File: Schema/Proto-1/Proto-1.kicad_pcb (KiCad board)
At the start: 2 copper layers, 71.5 x 29 mm, 5 parts, among them J1 Conn_02x03_Top_Bottom, U1 ATtiny85V-10P

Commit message: Benenne Files um
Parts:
- J1: value Conn_02x03_Top_Bottom -> Conn_02x03
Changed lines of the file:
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@@
 		)
 	)
-	(property "Version" "P1-0.3")
+	(property "Version" "P1-0.4a")
 	(net 0 "")
 	(net 1 "Net-(D1-DIN)")
@@
 		(property ki_fp_filters "DIP*W7.62mm*")
 		(sheetname "/")
-		(sheetfile "Spice.kicad_sch")
+		(sheetfile "Proto-1.kicad_sch")
 		(attr smd)
 		(fp_line
@@
 			)
 		)
-		(property "Value" "Conn_02x03_Top_Bottom"
+		(property "Value" "Conn_02x03"
 			(at 6.215 11.18 0)
 			(layer "F.Fab")
@@
 		(property ki_fp_filters "Connector*:*_2x??_*")
 		(sheetname "/")
-		(sheetfile "Spice.kicad_sch")
+		(sheetfile "Proto-1.kicad_sch")
 		(attr through_hole)
 		(fp_line
@@
 		(property ki_fp_filters "LED*WS2812*PLCC*5.0x5.0mm*P3.2mm*")
 		(sheetname "/")
-		(sheetfile "Spice.kicad_sch")
+		(sheetfile "Proto-1.kicad_sch")
 		(attr smd)
 		(fp_line
@@
 		(property ki_fp_filters "LED*WS2812*PLCC*5.0x5.0mm*P3.2mm*")
 		(sheetname "/")
-		(sheetfile "Spice.kicad_sch")
+		(sheetfile "Proto-1.kicad_sch")
 		(attr smd)
 		(fp_line
@@
 		(property ki_fp_filters "LED*WS2812*PLCC*5.0x5.0mm*P3.2mm*")
 		(sheetname "/")
-		(sheetfile "Spice.kicad_sch")
+		(sheetfile "Proto-1.kicad_sch")
 		(attr smd)
 		(fp_line

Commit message: Erstelle Schema für B
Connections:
- J1 pad 4: unconnected-(J1-Pin_4-Pad4) -> Reset
- U1 pad 1: unconnected-(U1-~{RESET}/PB5-Pad1) -> Reset
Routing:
- net Reset: track 0.00 -> 32.0 mm
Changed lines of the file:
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@@
 	(net 8 "SDA{slash}MOSI")
 	(net 9 "SCL{slash}MISO")
-	(net 10 "unconnected-(J1-Pin_4-Pad4)")
-	(net 11 "unconnected-(U1-~{RESET}{slash}PB5-Pad1)")
-	(net 12 "unconnected-(U1-XTAL2{slash}PB4-Pad3)")
+	(net 10 "Reset")
+	(net 11 "unconnected-(U1-XTAL2{slash}PB4-Pad3)")
 	(footprint "Package_SO:SO-8_3.9x4.9mm_P1.27mm"
 		(layer "F.Cu")
@@
 			(layers "F.Cu" "F.Mask" "F.Paste")
 			(roundrect_rratio 0.25)
-			(net 11 "unconnected-(U1-~{RESET}{slash}PB5-Pad1)")
+			(net 10 "Reset")
 			(pinfunction "~{RESET}/PB5")
-			(pintype "bidirectional+no_connect")
+			(pintype "bidirectional")
 		)
 		(pad "2" smd roundrect
@@
 			(layers "F.Cu" "F.Mask" "F.Paste")
 			(roundrect_rratio 0.25)
-			(net 12 "unconnected-(U1-XTAL2{slash}PB4-Pad3)")
+			(net 11 "unconnected-(U1-XTAL2{slash}PB4-Pad3)")
 			(pinfunction "XTAL2/PB4")
 			(pintype "bidirectional+no_connect")
@@
 			(layers "*.Cu" "*.Mask")
 			(remove_unused_layers no)
-			(net 10 "unconnected-(J1-Pin_4-Pad4)")
+			(net 10 "Reset")
 			(pinfunction "Pin_4")
-			(pintype "passive+no_connect")
+			(pintype "passive")
 		)
 		(pad "5" thru_hole circle
@@
 		(net 9)
 	)
+	(segment
+		(start 121 70.5)
+		(end 120.23 69.73)
+		(width 0.4)
+		(layer "F.Cu")
+		(net 10)
+	)
+	(segment
+		(start 137 72.5)
+		(end 137 75.5)
+		(width 0.4)
+		(layer "F.Cu")
+		(net 10)
+	)
+	(segment
+		(start 121 76.5)
+		(end 121 70.5)
+		(width 0.4)
+		(layer "F.Cu")
+		(net 10)
+	)
+	(segment
+		(start 120.23 69.73)
+		(end 118.35 69.73)
+		(width 0.4)
+		(layer "F.Cu")
+		(net 10)
+	)
+	(segment
+		(start 134 72.04)
+		(end 136.54 72.04)
+		(width 0.4)
+		(layer "F.Cu")
+		(net 10)
+	)
+	(segment
+		(start 135.5 77)
+		(end 121.5 77)
+		(width 0.4)
+		(layer "F.Cu")
+		(net 10)
+	)
+	(segment
+		(start 137 75.5)
+		(end 135.5 77)
+		(width 0.4)
+		(layer "F.Cu")
+		(net 10)
+	)
+	(segment
+		(start 136.54 72.04)
+		(end 137 72.5)
+		(width 0.4)
+		(layer "F.Cu")
+		(net 10)
+	)
+	(segment
+		(start 121.5 77)
+		(end 121 76.5)
+		(width 0.4)
+		(layer "F.Cu")
+		(net 10)
+	)
 	(zone

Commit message: Beginne Devboard
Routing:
- added copper zone on B.Cu, net GND
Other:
- board text removed: "P1-0.3a"
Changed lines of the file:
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@@
 		(layer "Edge.Cuts")
-	)
-	(gr_text "P1-0.3a"
-		(at 73.5 54 0)
-		(layer "F.SilkS")
-		(effects
-			(font
-				(size 1 1)
-				(thickness 0.1)
-			)
-			(justify left bottom)
-		)
 	)
 	(gr_text "${Version}"
@@
 			)
 		)
+	)
+	(zone
+		(net 2)
+		(net_name "GND")
+		(layer "B.Cu")
+		(hatch edge 0.5)
+		(priority 2)
+		(connect_pads
+			(clearance 0.5)
+		)
+		(min_thickness 0.25)
+		(filled_areas_thickness no)
+		(fill yes
+			(thermal_gap 0.5)
+			(thermal_bridge_width 0.5)
+		)
+		(polygon
+			(pts
+				(xy 71 57) (xy 142.5 57) (xy 142.5 86) (xy 71 86)
+			)
+		)

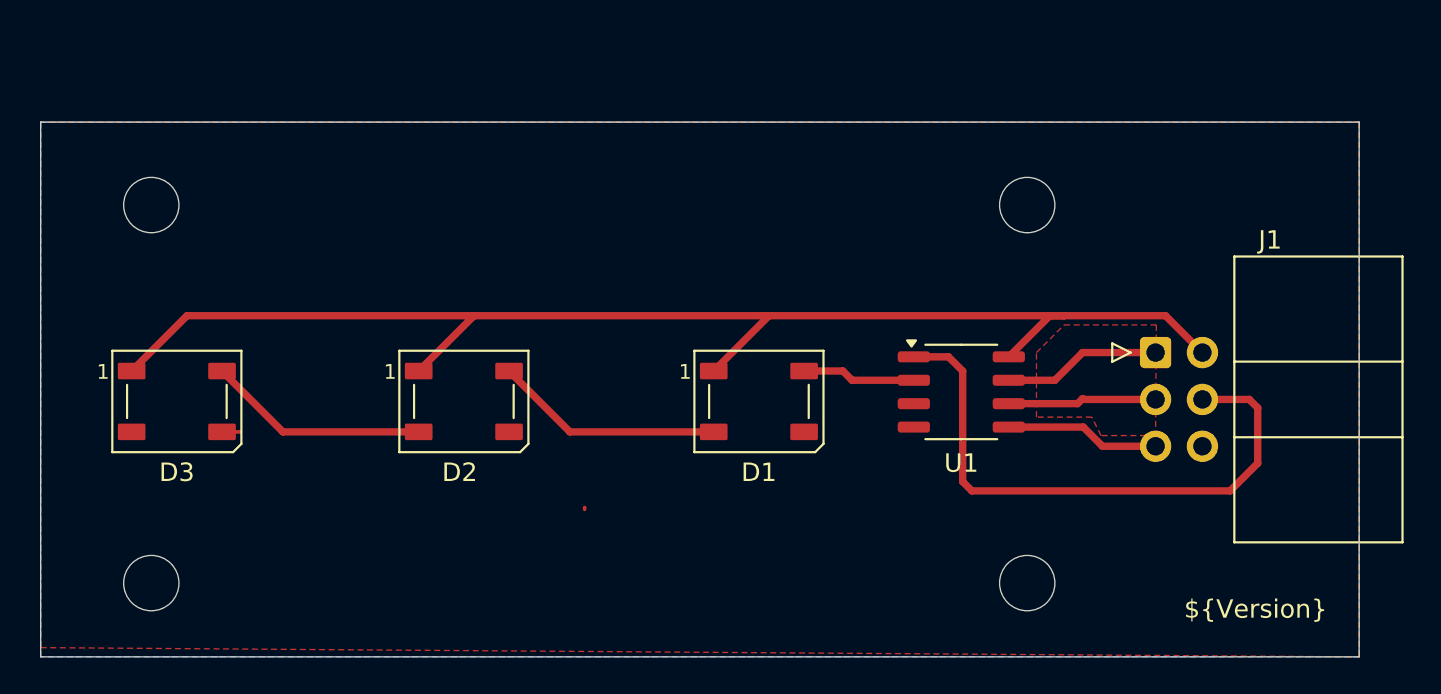
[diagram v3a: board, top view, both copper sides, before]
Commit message: Erstelle PCB für Devboard, ersetzte Proto-1-Board
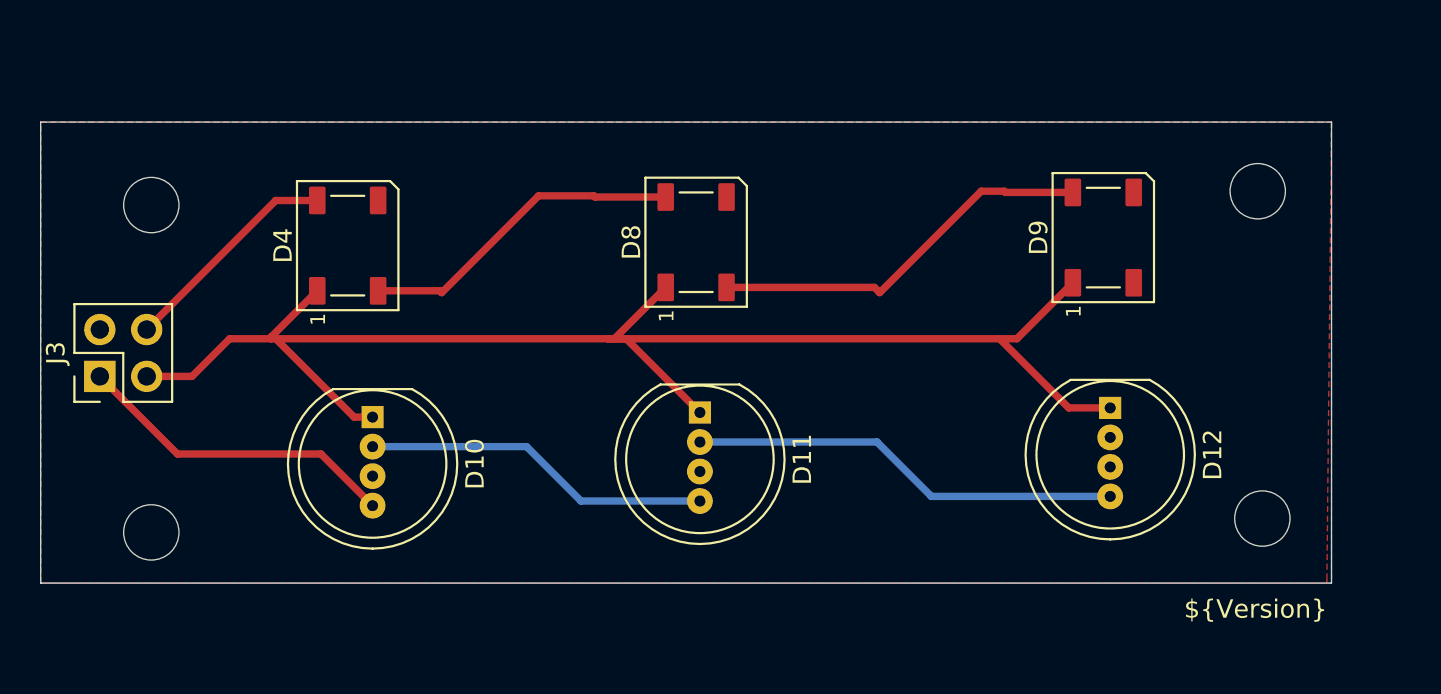
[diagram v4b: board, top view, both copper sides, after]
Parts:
- removed D1, D2, D3: WS2812B, LED_SMD:LED_WS2812B_PLCC4_5.0x5.0mm_P3.2mm
- removed J1: Conn_02x03, Connector_IDC:IDC-Header_2x03_P2.54mm_Horizontal
- removed U1: ATtiny85V-10P, Package_SO:SO-8_3.9x4.9mm_P1.27mm
- added D10: LED_THT-OSTWMN8132A, helclock:LED_D8.0mm-4, F.Cu at (89.0, 73.0)
- added D11: LED_THT-OSTWMN8132A, helclock:LED_D8.0mm-4, F.Cu at (106.8, 72.8)
- added D12: LED_THT-OSTWMN8132A, helclock:LED_D8.0mm-4, F.Cu at (129.0, 72.5)
- added D4: LED-Brightek, helclock:LED-SMD-Brightek-N0M50S18IC_5.0x5.0mm_P3.2mm, F.Cu at (87.7, 63.7)
- added D8: LED-Brightek, helclock:LED-SMD-Brightek-N0M50S18IC_5.0x5.0mm_P3.2mm, F.Cu at (106.5, 63.5)
- added D9: LED-Brightek, helclock:LED-SMD-Brightek-N0M50S18IC_5.0x5.0mm_P3.2mm, F.Cu at (128.6, 63.3)
- added J3: Conn_02x02_Counter_Clockwise, Connector_PinHeader_2.54mm:PinHeader_2x02_P2.54mm_Vertical, F.Cu at (74.2, 70.8)
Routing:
- net Reset: track 32.0 -> 0.00 mm
- net Net-(D11-DOUT): track 0.00 -> 23.5 mm
- net Net-(D8-DOUT): track 0.00 -> 21.2 mm
- net Net-(D10-DOUT): track 0.00 -> 19.0 mm
- net Net-(D4-DOUT): track 0.00 -> 17.8 mm
- net Net-(D10-DIN): track 0.00 -> 17.7 mm
- net Net-(D1-DOUT): track 12.5 -> 0.00 mm
- net Net-(D4-DIN): track 0.00 -> 12.1 mm
- net Net-(D2-DOUT): track 12.0 -> 0.00 mm
- net SCK: track 8.58 -> 0.00 mm
- net +5V: track 72.5 -> 81.1 mm
- net SDA/MOSI: track 8.39 -> 0.00 mm
- net SCL/MISO: track 8.09 -> 0.00 mm
- net Net-(D1-DIN): track 6.16 -> 0.00 mm
- net GND: track 1.06 -> 0.00 mm
- removed copper zone on F.Cu, net (none)
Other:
- board size 71.5 x 29 mm -> 70 x 25 mm

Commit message: Bereite DB1-0.4 vor
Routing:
- net GND: track 0.00 -> 76.8 mm
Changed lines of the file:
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@@
 		(tenting front back)
 		(pcbplotparams
-			(layerselection 0x00000000_00000000_55555555_55555551)
+			(layerselection 0x00000000_00000000_55555555_55555555)
 			(plot_on_all_layers_selection 0x00000000_00000000_00000000_00000000)
 			(disableapertmacros no)
@@
 		)
 	)
-	(property "Version" "P1-0.4a")
+	(property "Version" "DB1-0.4")
 	(net 0 "")
 	(net 1 "Net-(D4-DOUT)")
@@
 	)
 	(gr_text "${Version}"
-		(at 133 84 0)
+		(at 112.75 60.75 0)
 		(layer "F.SilkS")
 		(effects
@@
 		)
 	)
+	(gr_text "${Version}"
+		(at 120 61 0)
+		(layer "B.SilkS")
+		(effects
+			(font
+				(size 1 1)
+				(thickness 0.1)
+			)
+			(justify left bottom mirror)
+		)
+	)
+	(dimension
+		(type orthogonal)
+		(layer "Dwgs.User")
+		(pts
+			(xy 141 57) (xy 71 57)
+		)
+		(height -6.25)
+		(orientation 0)
+		(format
+			(prefix "")
+			(suffix "")
+			(units 3)
+			(units_format 0)
+			(precision 4)
+			(suppress_zeroes yes)
+		)
+		(style
+			(thickness 0.1)
+			(arrow_length 1.27)
+			(text_position_mode 0)
+			(arrow_direction outward)
+			(extension_height 0.58642)
+			(extension_offset 0.5)
+			(keep_text_aligned yes)
+		)
+		(gr_text "70"
+			(at 106 49.6 0)
+			(layer "Dwgs.User")
+			(effects
+				(font
+					(size 1 1)
+					(thickness 0.15)
+				)
+			)
+		)
+	)
+	(dimension
+		(type orthogonal)
+		(layer "Dwgs.User")
+		(pts
+			(xy 141 57) (xy 141 82)
+		)
+		(height 7.25)
+		(orientation 1)
+		(format
+			(prefix "")
+			(suffix "")
+			(units 3)
+			(units_format 0)
+			(precision 4)
+			(suppress_zeroes yes)
+		)
+		(style
+			(thickness 0.1)
+			(arrow_length 1.27)
+			(text_position_mode 0)
+			(arrow_direction outward)
+			(extension_height 0.58642)
+			(extension_offset 0.5)
+			(keep_text_aligned yes)
+		)
+		(gr_text "25"
+			(at 147.1 69.5 90)
+			(layer "Dwgs.User")
+			(effects
+				(font
+					(size 1 1)
+					(thickness 0.15)
+				)
+			)
+		)
+	)
 	(segment
 		(start 101.065 61.065)
@@
 	)
 	(segment
+		(start 84.25 72)
+		(end 84.25 73.25)
+		(width 0.4)
+		(layer "B.Cu")
+		(net 2)
+	)
+	(segment
+		(start 78.25 66)
+		(end 82.75 70.5)
+		(width 0.4)
+		(layer "B.Cu")
+		(net 2)
+	)
+	(segment
+		(start 101.3 70.5)
+		(end 123.8 70.5)
+		(width 0.4)
+		(layer "B.Cu")
+		(net 2)
+	)
+	(segment
+		(start 84.25 73.25)
+		(end 86.05 73.25)
+		(width 0.4)
+		(layer "B.Cu")
+		(net 2)
+	)
+	(segment
+		(start 76.46 66)
+		(end 78.25 66)
+		(width 0.4)
+		(layer "B.Cu")
+		(net 2)
+	)
+	(segment
+		(start 86.05 73.25)
+		(end 89 76.2)
+		(width 0.4)
+		(layer "B.Cu")
+		(net 2)
+	)
+	(segment
+		(start 101.3 70.5)
+		(end 106.75 75.95)
+		(width 0.4)
+		(layer "B.Cu")
+		(net 2)
+	)
+	(segment
+		(start 82.75 70.5)
+		(end 84.25 72)
+		(width 0.4)
+		(layer "B.Cu")
+		(net 2)
+	)
+	(segment
+		(start 82.75 70.5)
+		(end 101.3 70.5)
+		(width 0.4)
+		(layer "B.Cu")
+		(net 2)
+	)
+	(segment
+		(start 74.21 68.25)
+		(end 76.46 66)
+		(width 0.4)
+		(layer "B.Cu")
+		(net 2)
+	)
+	(segment
+		(start 123.8 70.5)
+		(end 129 75.7)
+		(width 0.4)
+		(layer "B.Cu")
+		(net 2)
+	)
+	(segment
 		(start 123.94 68.75)
 		(end 126.975 65.715)
@@
 	)
 	(zone
+		(net 2)
+		(net_name "GND")
+		(layer "F.Cu")
+		(hatch edge 0.5)
+		(priority 2)
+		(connect_pads
+			(clearance 0.5)
+		)
+		(min_thickness 0.25)
+		(filled_areas_thickness no)
+		(fill yes
+			(thermal_gap 0.5)
+			(thermal_bridge_width 0.5)
+		)
+		(polygon
+			(pts
+				(xy 77 72.25) (xy 80 71) (xy 81.75 69.25) (xy 83.5 69.25) (xy 87.25 73) (xy 89 75.54) (xy 78.75 75.54)
+			)
+		)
+	)
+	(zone
